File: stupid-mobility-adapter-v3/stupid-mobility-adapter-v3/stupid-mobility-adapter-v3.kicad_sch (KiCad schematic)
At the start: 35 parts, among them J1 BTS7968-0, J2 Act0-FB, J3 BTS7968-1, J4 Act1-FB, J5 ESTOP_INPUT, J6 UART, J7 Relays, J8 I2C, J9 BATT_MON_SELECT, Q1 2N3904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

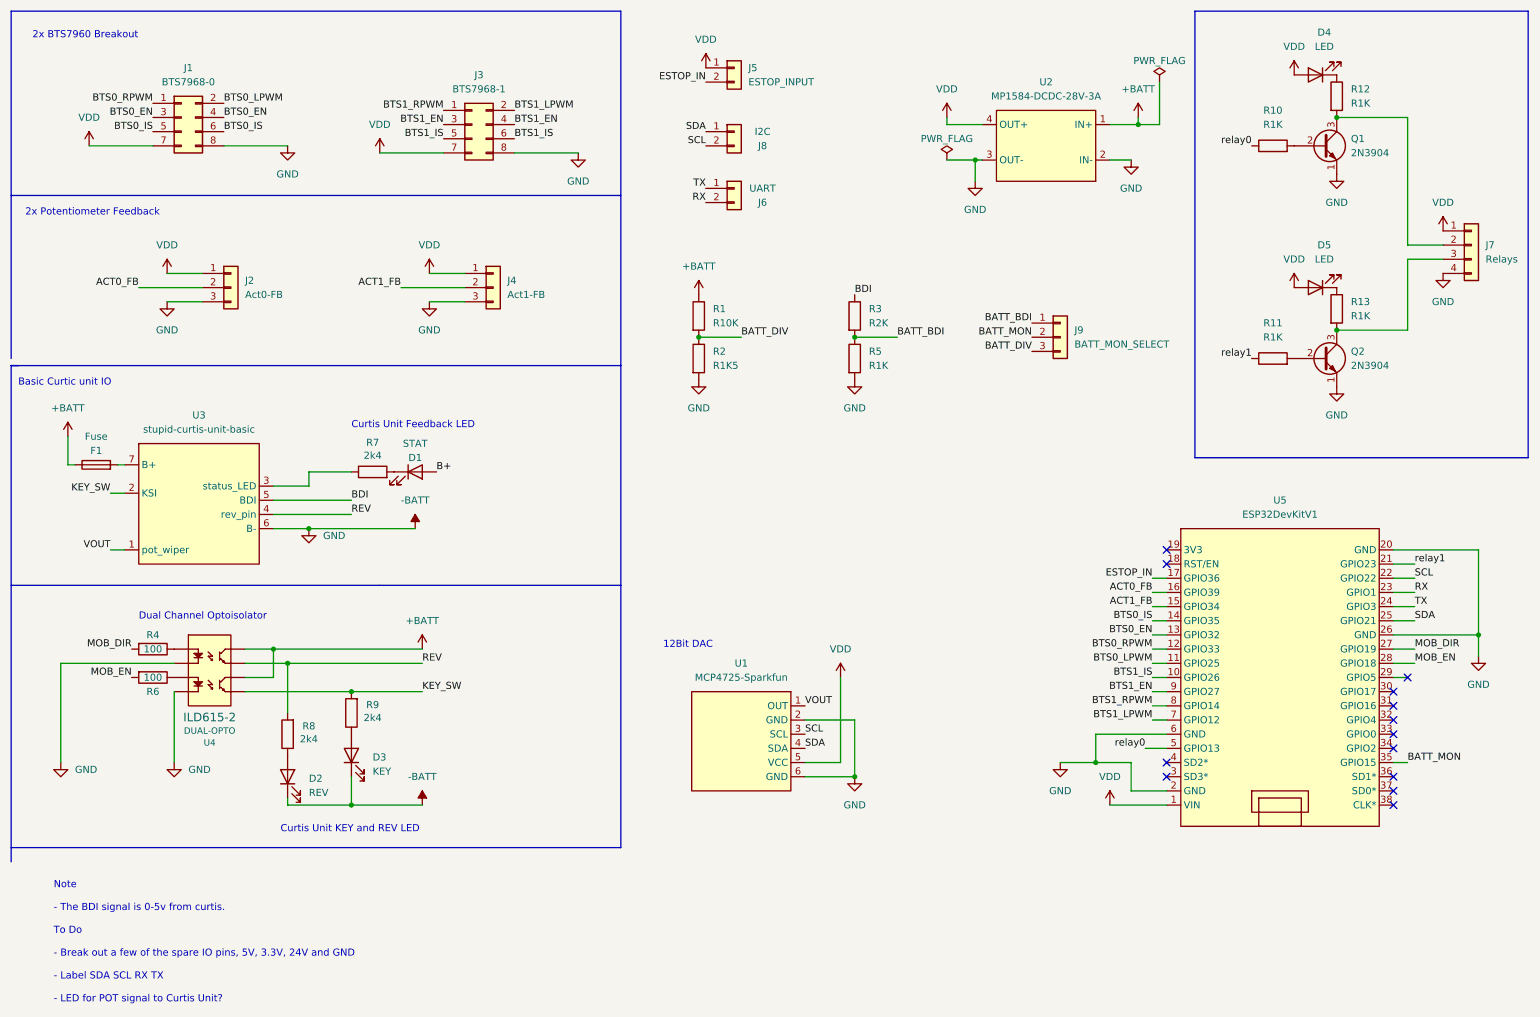
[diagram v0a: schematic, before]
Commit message: Added buzzer and servo input to v3 pcb
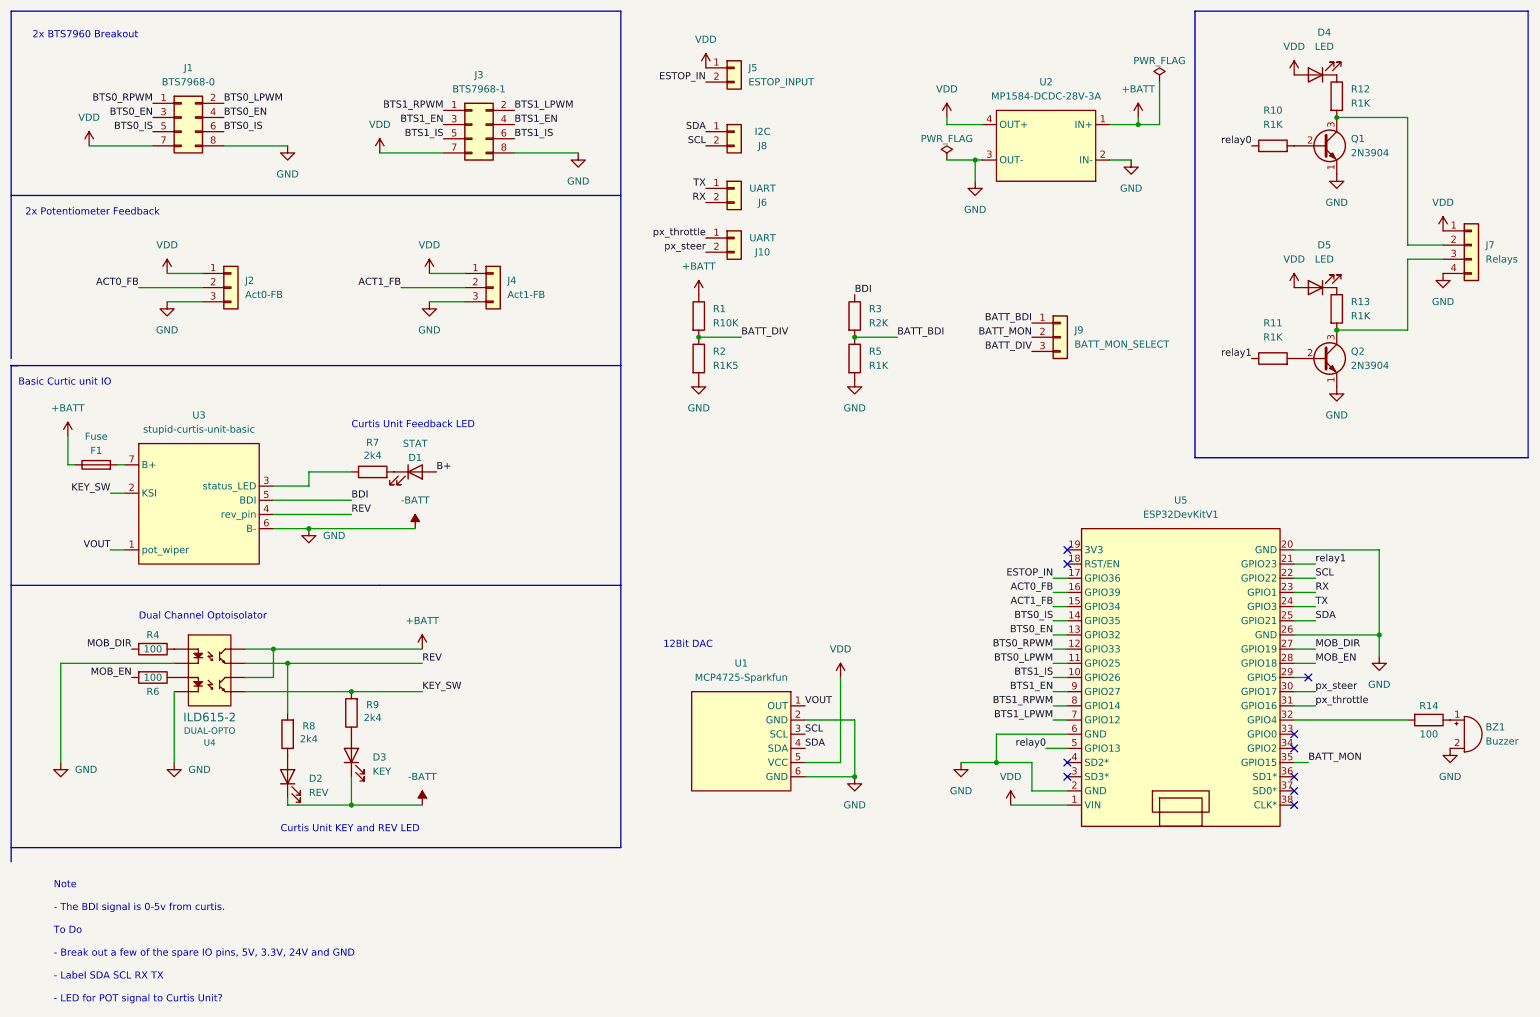
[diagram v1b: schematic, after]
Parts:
- added BZ1: Buzzer, stuipid-electronics-components:Buzzer_ABT-460-RC, symbol Device:Buzzer
- added J10: UART, Connector_PinHeader_2.54mm:PinHeader_1x02_P2.54mm_Vertical, symbol Connector_Generic:Conn_01x02
- added R14: 100, Resistor_THT:R_Axial_DIN0207_L6.3mm_D2.5mm_P7.62mm_Horizontal, symbol Device:R
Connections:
- net -BATT: now also BZ1.2 (+)
- net px_steer: now reaches U5.30 (GPIO17)
- net px_steer: now also J10.2 (Pin_2)
- net px_throttle: now reaches U5.31 (GPIO16)
- net px_throttle: now also J10.1 (Pin_1)
- net at U5.32 (GPIO4): now also R14.2
- new net: BZ1.1 (-), R14.1
- no-connect marks 13 -> 10
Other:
- moved on the sheet: U5
